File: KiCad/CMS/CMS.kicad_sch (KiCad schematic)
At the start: 15 parts, among them U1 LTC6090, U2 LTC6090

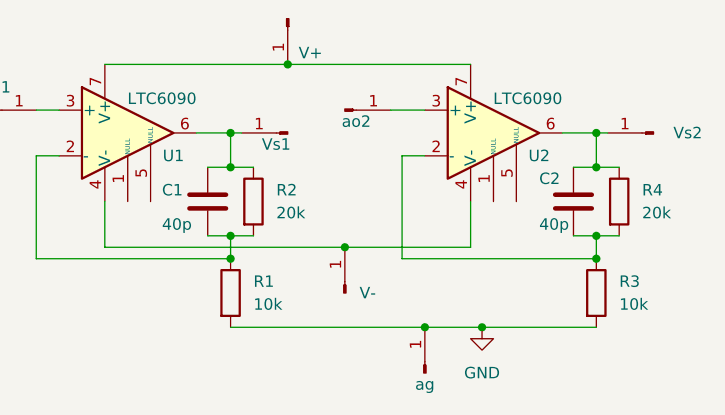
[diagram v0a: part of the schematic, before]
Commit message: Added CMS ampli
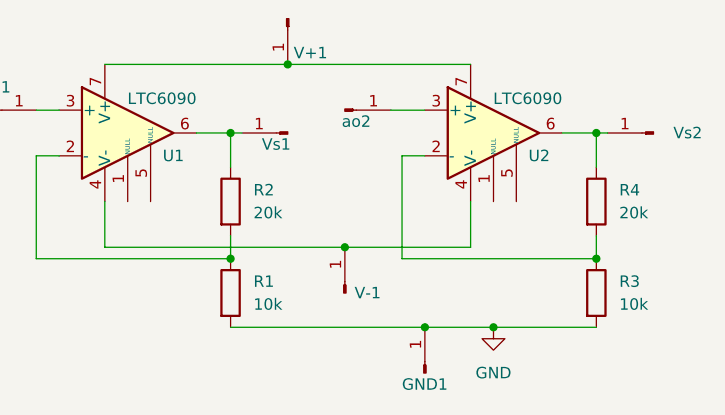
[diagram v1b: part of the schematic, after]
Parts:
- removed C1, C2: 40p, Capacitor_THT:C_Disc_D5.0mm_W2.5mm_P2.50mm, symbol Device:C
- U1, U2: footprint Package_DIP:DIP-8_W7.62mm -> Package_SO:SOIC-8_3.9x4.9mm_P1.27mm
- renumbered ag to GND1, V+ to V+1, V- to V-1
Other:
- moved on the sheet: R2, R4

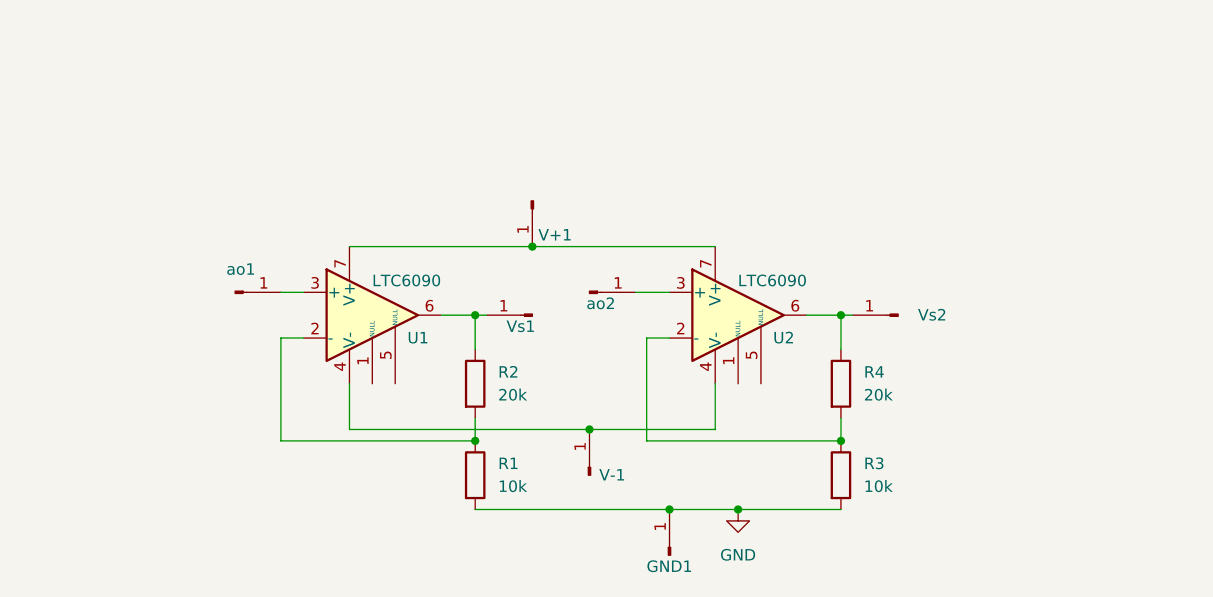
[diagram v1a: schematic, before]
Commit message: Better schematics + 3D models + New images
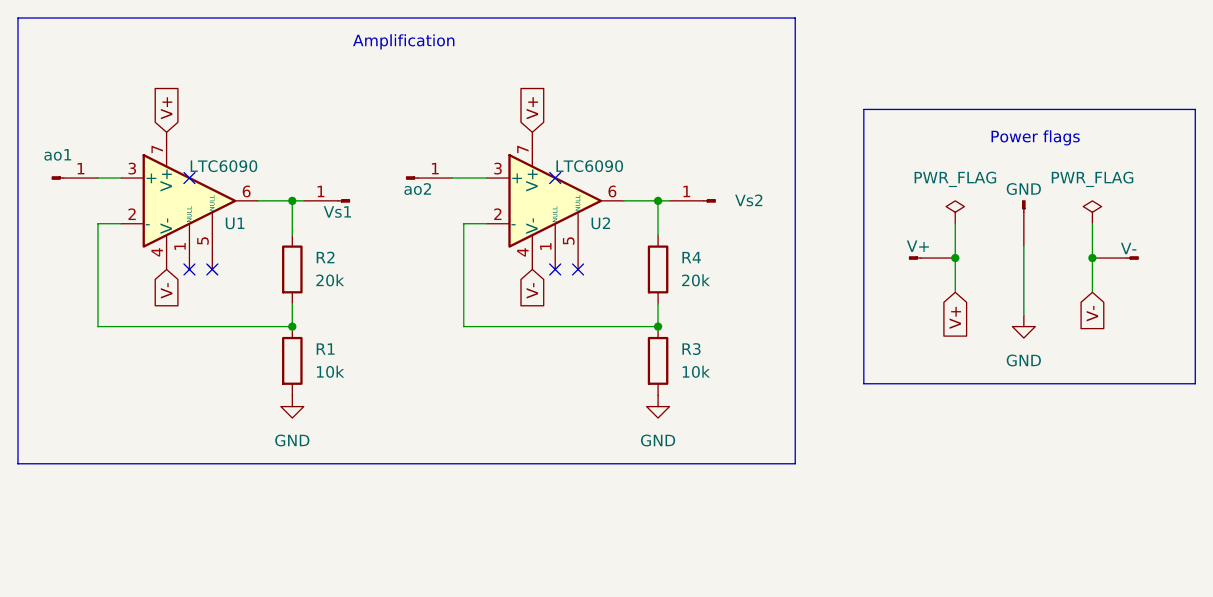
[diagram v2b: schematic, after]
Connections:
- net V-: now reaches U1.4 (V-), U2.4 (V-), V-1.1 (Pin_1)
- net V+: now reaches U1.7 (V+), U2.7 (V+), V+1.1 (Pin_1)
- no-connect marks 0 -> 6
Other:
- note added: "Amplification"
- note added: "Power flags"
- moved on the sheet: R1, R2, R3, R4, U1, U2, Vs1, Vs2, ao1, ao2
